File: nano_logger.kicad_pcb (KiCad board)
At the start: 2 copper layers, 38.1 x 25.4 mm, 17 parts, among them CON1 AVR-ISP-6, IC1 ATMEGA328P-M, P1 SDMICRO, P2 P1, P3 FTDI, Y1 RESONATORSMD

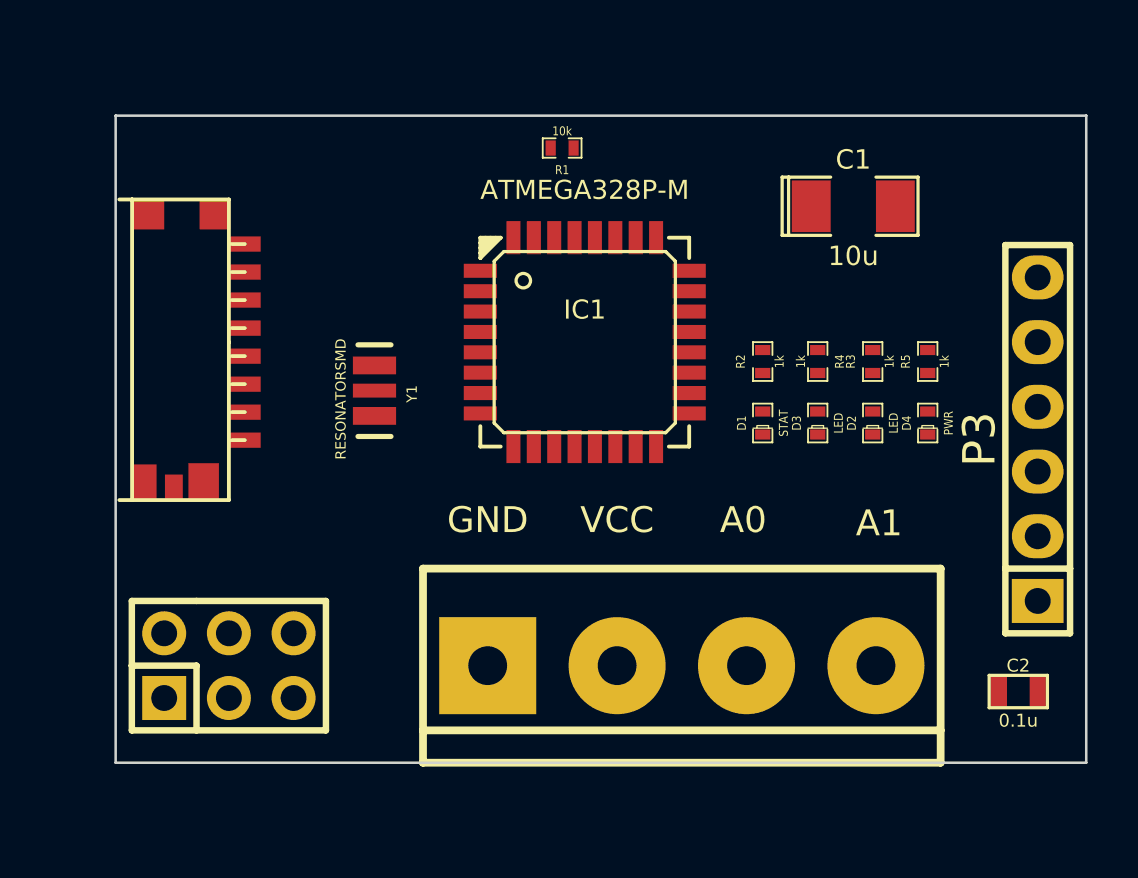
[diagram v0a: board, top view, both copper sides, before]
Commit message: Fixed atmega footprint
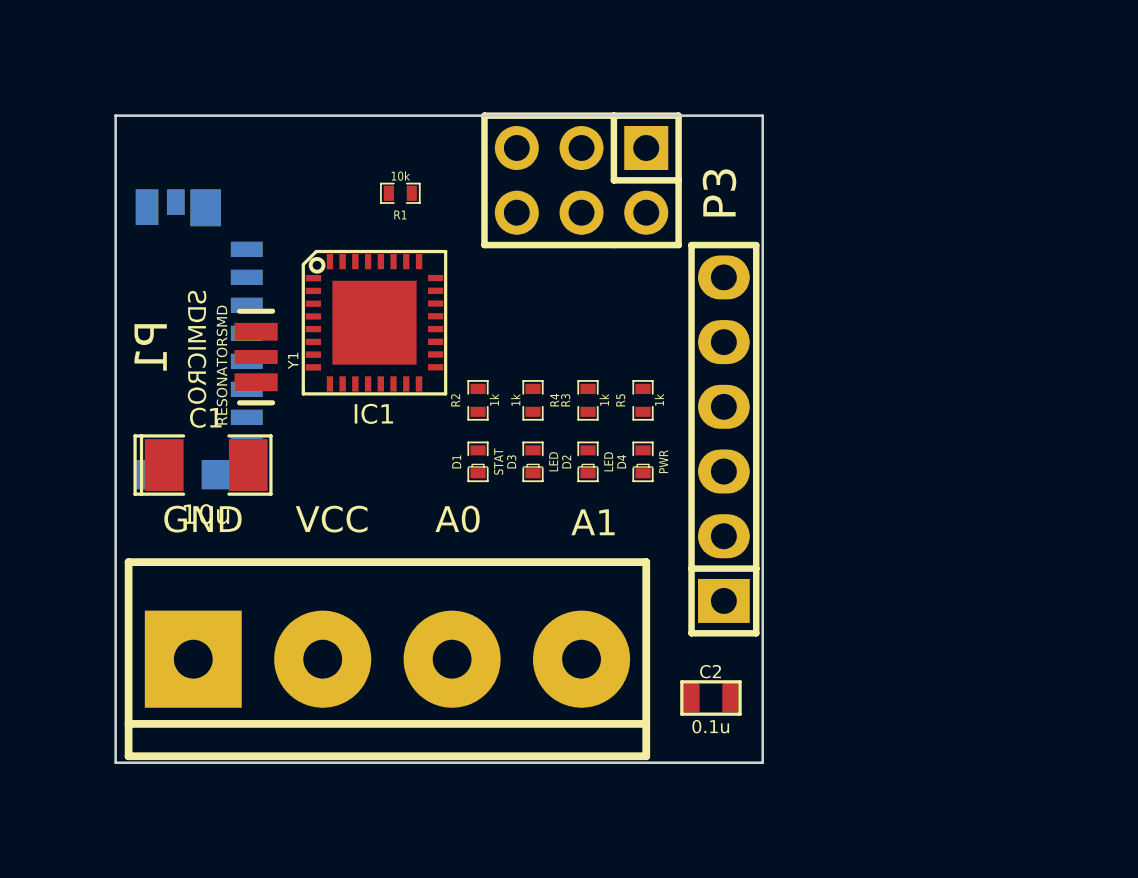
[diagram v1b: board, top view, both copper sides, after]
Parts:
- IC1: footprint QFP:lqfp32 -> SMD_Packages:QFN32-5x5
- P1: moved to B.Cu
- moved C1 27.4 mm to (29.0, 39.1)
- moved CON1 23.5 mm to (43.7, 27.9), turned to 180 degrees
- moved P3 12.3 mm to (49.3, 38.1)
- moved C2 12.1 mm to (48.8, 48.3)
- moved P2 11.6 mm to (36.1, 46.7)
- moved R3 11.3 mm to (43.9, 36.6)
- moved R4 11.3 mm to (41.8, 36.6)
- moved R5 11.3 mm to (46.1, 36.6)
- moved D2 11.3 mm to (43.9, 39.0)
- moved D3 11.3 mm to (41.8, 39.0)
- moved D4 11.3 mm to (46.1, 39.0)
- moved R2 11.3 mm to (39.6, 36.6)
- moved D1 11.3 mm to (39.6, 39.0)
- moved IC1 8.29 mm to (35.6, 33.5), turned to 0 degrees
- moved R1 6.59 mm to (36.6, 28.4)
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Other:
- board size 38.1 x 25.4 mm -> 25.4 x 25.4 mm

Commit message: Moved parts around and routed
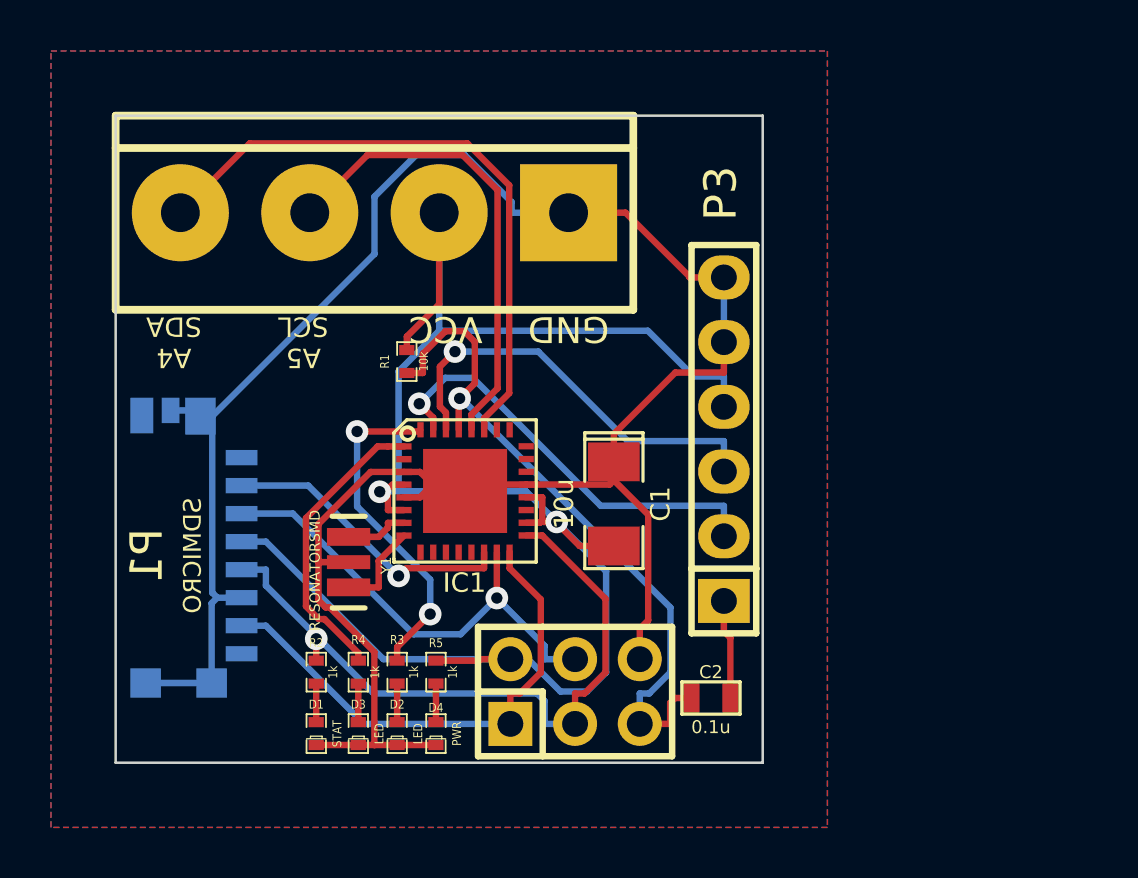
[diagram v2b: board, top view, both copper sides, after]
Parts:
- moved CON1 20.1 mm to (43.4, 48.0), turned to 0 degrees
- moved P2 17.5 mm to (35.6, 29.2), turned to 180 degrees
- moved C1 16.1 mm to (45.0, 40.6), turned to 270 degrees
- moved D4 13.4 mm to (38.0, 49.7)
- moved R5 13.4 mm to (38.0, 47.2)
- moved D2 13.0 mm to (36.4, 49.7)
- moved R3 13.0 mm to (36.4, 47.2)
- moved D3 12.7 mm to (34.9, 49.7)
- moved R4 12.7 mm to (34.9, 47.2), turned to 270 degrees
- moved D1 12.4 mm to (33.3, 49.7)
- moved R2 12.4 mm to (33.3, 47.2)
- moved Y1 8.83 mm to (34.5, 42.9)
- moved P1 8.18 mm to (29.7, 42.7)
- moved IC1 7.50 mm to (39.1, 40.1)
- moved R1 6.61 mm to (36.8, 35.1), turned to 270 degrees
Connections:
- IC1 pad 23: ADC0 -> Net-(IC1-Pad23)
- IC1 pad 24: ADC1 -> Net-(IC1-Pad24)
- IC1 pad 27: Net-(IC1-Pad27) -> ADC4
- IC1 pad 28: Net-(IC1-Pad28) -> ADC5
- P2 pad 3: ADC0 -> ADC5
- P2 pad 4: ADC1 -> ADC4
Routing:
- net GND: track 0.00 -> 92.2 mm
- net VCC: track 0.00 -> 72.7 mm, vias 0 -> 2
- net RESET: track 0.00 -> 27.6 mm, vias 0 -> 1
- net SCLK: track 0.00 -> 27.2 mm, vias 0 -> 1
- net ADC4: track 0.00 -> 24.7 mm
- net MISO: track 0.00 -> 20.1 mm
- net MOSI: track 0.00 -> 18.7 mm, vias 0 -> 1
- net ADC5: track 0.00 -> 18.7 mm
- net TXD: track 0.00 -> 16.9 mm, vias 0 -> 1
- net RXD: track 0.00 -> 16.6 mm, vias 0 -> 1
- net D2: track 0.00 -> 13.2 mm, vias 0 -> 2
- net CS: track 0.00 -> 11.7 mm, vias 0 -> 1
- net D3: track 0.00 -> 11.6 mm
- net DTR: track 0.00 -> 3.92 mm
- net Net-(IC1-Pad8): track 0.00 -> 3.62 mm
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- added copper zone on B.Cu, net GND
- added copper zone on F.Cu, net GND
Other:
- net class Default: clearance 0.254 -> 0.2032
- rule trace_clearance: 0.254 -> 0.2032
- rule trace_min: 0.254 -> 0.1524
- board text added: "2014 Visgence Inc Nano Logger"
- board text added: "A4 SDA"
- board text added: "A5 SCL"
- board text removed: "A0"
- board text removed: "A1"
